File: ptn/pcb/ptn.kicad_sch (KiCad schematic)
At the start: 100 parts, among them IC1 ADP150AUJZ-3.3-R7, IC2 AZ1084CD-5.0TRG1, IC3 GRF5509, J1 TB002-500-04BE, J2 Conn_02x12_Counter_Clockwise, J3 NRF_CONN, J4 142-0701-801, J5 Conn_01x04, SW1 SW_Push, U1 NCP1117-3.3_SOT223, U2 ADF4351, U3 STM32F103C8T6, U4 MCP2551-I-SN, Y1 SIT5000AICGE-33E0-25.000000X, Y2 16MHz

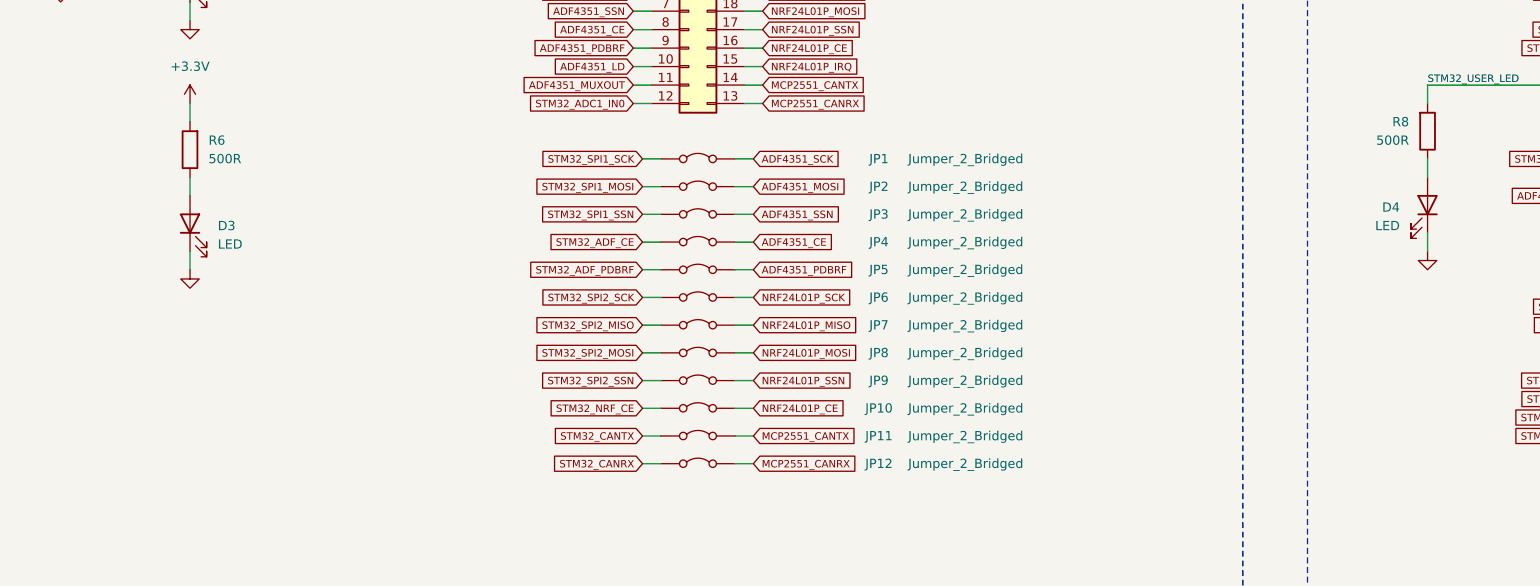
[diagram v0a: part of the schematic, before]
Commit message: Add correct LED resistances
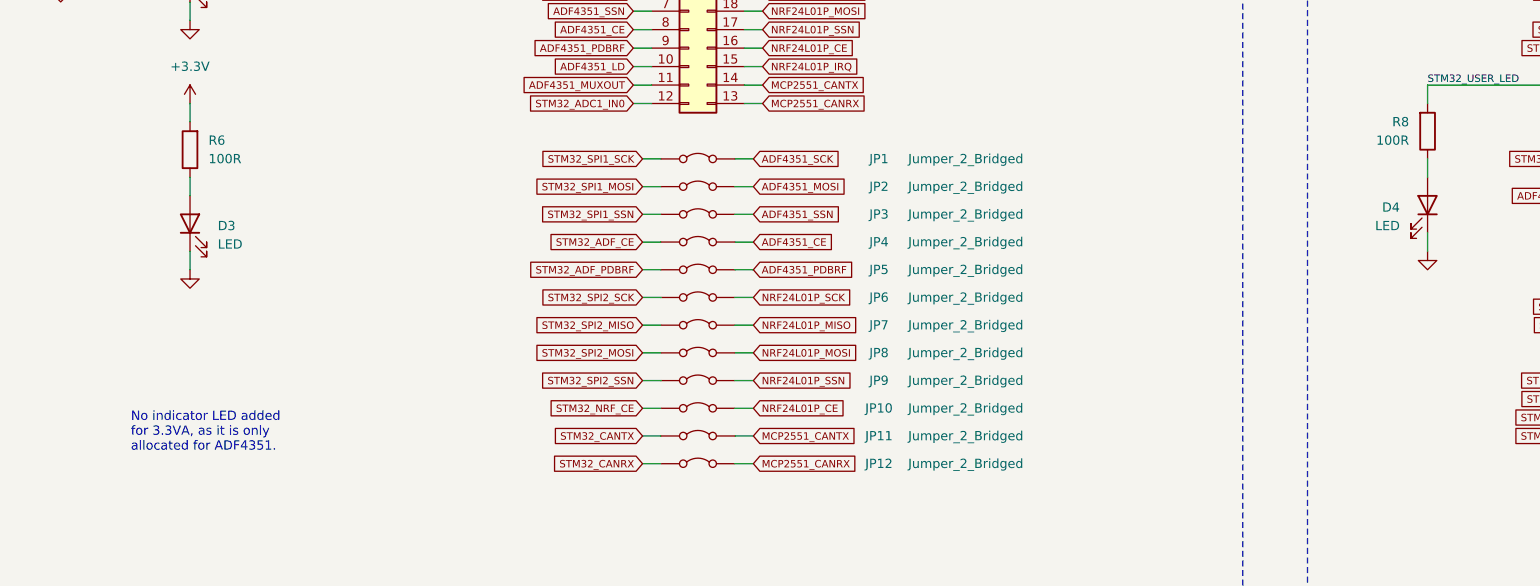
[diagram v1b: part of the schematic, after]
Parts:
- R6, R8: value 500R -> 100R
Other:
- note added: "No indicator LED added for 3.3VA, as it is only allocated for ADF4351."
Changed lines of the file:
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@@
 		)
 	)
+	(text "No indicator LED added\nfor 3.3VA, as it is only\nallocated for ADF4351."
+		(exclude_from_sim no)
+		(at 151.892 139.192 0)
+		(effects
+			(font
+				(size 1.27 1.27)
+			)
+			(justify left)
+		)
+	)
 	(text "Note: Check SW is needed or not."
 		(exclude_from_sim no)
@@
 			)
 		)
-		(property "Value" "500R"
+		(property "Value" "100R"
 			(at 327.66 99.0599 0)
 			(effects
@@
 			)
 		)
-		(property "Value" "500R"
+		(property "Value" "100R"
 			(at 162.56 101.5999 0)
 			(effects
@@
 			)
 		)
-		(property "Description" "Light emitting diode"
+		(property "Description" "Light emitting diode 150060VS55040"
 			(at 160.02 76.2 0)
 			(effects
@@
 			)
 		)
-		(property "Description" "Light emitting diode"
+		(property "Description" "Light emitting diode 150060VS55040"
 			(at 330.2 107.95 0)
 			(effects
@@
 			)
 		)
-		(property "Description" "Light emitting diode"
+		(property "Description" "Light emitting diode 150060VS55040"
 			(at 160.02 110.49 0)
 			(effects

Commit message: Footprint assignment
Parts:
- added C35, C36, C38, C42, C44, C46, C50, C51, C52: ~, symbol Device:C
- added C40: 0.1u, Capacitor_SMD:C_0402_1005Metric, symbol Device:C
- added R12: 0R, symbol Device:R
- C1, C5, C8: footprint (none) -> Capacitor_SMD:C_0805_2012Metric; Manufacturer_Name (none) -> Murata Electronics; Manufacturer_Part_Number (none) -> GRM21BR61E106KA73K; Mouser Part Number (none) -> 81-GRM21BR61E106KA3K
- C10: footprint (none) -> Capacitor_SMD:C_0805_2012Metric; Manufacturer_Name (none) -> Murata Electronics; Manufacturer_Part_Number (none) -> GRM21BR61E226ME44K; Mouser Part Number (none) -> 81-GRM21BR61E226ME4K
- C11, C12, C15, C17, C18, C19, C23, C24, C25, C31: footprint (none) -> Capacitor_SMD:C_0402_1005Metric; Manufacturer_Name (none) -> Murata Electronics; Manufacturer_Part_Number (none) -> GCM1555C1H100JA16J; Mouser Part Number (none) -> 81-GCM1555C1H100JA6J
- C13, C14, C16, C20, C21, C22, C26, C27, C28, C32: footprint (none) -> Capacitor_SMD:C_0402_1005Metric; Manufacturer_Name (none) -> Murata Electronics; Manufacturer_Part_Number (none) -> GRM155R71C104JA88J; Mouser Part Number (none) -> 81-GRM155R71C104JA8J
- C2, C9: footprint (none) -> Capacitor_SMD:C_0603_1608Metric; Manufacturer_Name (none) -> KEMET; Manufacturer_Part_Number (none) -> C0603C105K3PACTU; Mouser Part Number (none) -> 80-C0603C105K3P
- C29, C30: footprint (none) -> Capacitor_SMD:C_0603_1608Metric; Manufacturer_Name (none) -> KYOCERA AVX; Manufacturer_Part_Number (none) -> 06035A102JAT2A; Mouser Part Number (none) -> 581-06035A102J
- C3: footprint (none) -> Capacitor_SMD:C_0603_1608Metric; Manufacturer_Name (none) -> KYOCERA AVX; Manufacturer_Part_Number (none) -> 06031C272JAT2A; Mouser Part Number (none) -> 581-06031C272JAT2A
- C33: footprint (none) -> Capacitor_SMD:C_0402_1005Metric; Guerrilla ID (none) -> M4; Manufacturer_Name (none) -> Murata Electronics; Manufacturer_Part_Number (none) -> GJM1555C1H5R6WB01D; Mouser Part Number (none) -> 81-GJM1555C1H5R6WB1D
- C34: value 0.1u -> ~; Guerrilla ID (none) -> M5; now not fitted
- C37: renamed from C35; value 100n -> 0.1u; footprint (none) -> Capacitor_SMD:C_0402_1005Metric; Manufacturer_Name (none) -> Murata Electronics; Manufacturer_Part_Number (none) -> GRM155R71C104JA88J; Mouser Part Number (none) -> 81-GRM155R71C104JA8J
- C39: renamed from C37; footprint (none) -> Capacitor_SMD:C_0805_2012Metric; Manufacturer_Name (none) -> Murata Electronics; Manufacturer_Part_Number (none) -> GRM21BR61E106KA73K; Mouser Part Number (none) -> 81-GRM21BR61E106KA3K
- C4: footprint (none) -> Capacitor_SMD:C_0603_1608Metric; Manufacturer_Name (none) -> KEMET; Manufacturer_Part_Number (none) -> C0603C473J3RACTU; Mouser Part Number (none) -> 80-C0603C473J3R
- C41: renamed from C40; value 100n -> 0.1u; footprint (none) -> Capacitor_SMD:C_0402_1005Metric; Manufacturer_Name (none) -> Murata Electronics; Manufacturer_Part_Number (none) -> GRM155R71C104JA88J; Mouser Part Number (none) -> 81-GRM155R71C104JA8J
- C43: renamed from C42; value 100n -> 0.1u; footprint (none) -> Capacitor_SMD:C_0402_1005Metric; Manufacturer_Name (none) -> Murata Electronics; Manufacturer_Part_Number (none) -> GRM155R71C104JA88J; Mouser Part Number (none) -> 81-GRM155R71C104JA8J
- C45: renamed from C43; value 100n -> 0.1u; footprint (none) -> Capacitor_SMD:C_0402_1005Metric; Manufacturer_Name (none) -> Murata Electronics; Manufacturer_Part_Number (none) -> GRM155R71C104JA88J; Mouser Part Number (none) -> 81-GRM155R71C104JA8J
- C47: renamed from C38; footprint (none) -> Capacitor_SMD:C_0402_1005Metric; Guerrilla ID (none) -> M14; Manufacturer_Name (none) -> Murata Electronics; Manufacturer_Part_Number (none) -> GRM155R71C104JA88J; Mouser Part Number (none) -> 81-GRM155R71C104JA8J
- C48: renamed from C39; footprint (none) -> Capacitor_SMD:C_0402_1005Metric; Guerrilla ID (none) -> M15; Manufacturer_Name (none) -> Murata Electronics; Manufacturer_Part_Number (none) -> GRM1555C1H101FA01D; Mouser Part Number (none) -> 81-GRM1555C1H101FA1D
- C49: renamed from C44; value 100n -> 0.1u; footprint (none) -> Capacitor_SMD:C_0402_1005Metric; Manufacturer_Name (none) -> Murata Electronics; Manufacturer_Part_Number (none) -> GRM155R71C104JA88J; Mouser Part Number (none) -> 81-GRM155R71C104JA8J
- C53: renamed from C36; footprint (none) -> Capacitor_SMD:C_0402_1005Metric; Guerrilla ID (none) -> M22; Manufacturer_Name (none) -> Murata Electronics; Manufacturer_Part_Number (none) -> GJM1555C1H120FB01D; Mouser Part Number (none) -> 81-GJM1555C1H120FB1D
- C54: renamed from C41; footprint (none) -> Capacitor_SMD:C_0402_1005Metric; Guerrilla ID (none) -> M23; Manufacturer_Name (none) -> Murata Electronics; Manufacturer_Part_Number (none) -> GJM1555C1H200FB01D; Mouser Part Number (none) -> 81-GJM1555C1H200FB1D
- C55: renamed from C45; footprint (none) -> Capacitor_SMD:C_0603_1608Metric; Manufacturer_Name (none) -> KEMET; Manufacturer_Part_Number (none) -> C0603C103J5RAC7411; Mouser Part Number (none) -> 80-C0603C103J5R7411
- C56: renamed from C46; footprint (none) -> Capacitor_SMD:C_0603_1608Metric; Manufacturer_Name (none) -> KEMET; Manufacturer_Part_Number (none) -> C0603C105K3PACTU; Mouser Part Number (none) -> 80-C0603C105K3P
- C57: renamed from C47; footprint (none) -> Capacitor_SMD:C_0402_1005Metric; Manufacturer_Name (none) -> Murata Electronics; Manufacturer_Part_Number (none) -> GCM1555C1H100JA16J; Mouser Part Number (none) -> 81-GCM1555C1H100JA6J
- C58: renamed from C48; footprint (none) -> Capacitor_SMD:C_0603_1608Metric; Manufacturer_Name (none) -> KEMET; Manufacturer_Part_Number (none) -> C0603C105K3PACTU; Mouser Part Number (none) -> 80-C0603C105K3P
- C59: renamed from C49; footprint (none) -> Capacitor_SMD:C_0402_1005Metric; Manufacturer_Name (none) -> Murata Electronics; Manufacturer_Part_Number (none) -> GCM1555C1H100JA16J; Mouser Part Number (none) -> 81-GCM1555C1H100JA6J
- C6: footprint (none) -> Capacitor_SMD:C_0402_1005Metric; Manufacturer_Name (none) -> Murata Electronics; Manufacturer_Part_Number (none) -> GRM1555C1H101FA01D; Mouser Part Number (none) -> 81-GRM1555C1H101FA1D
- C7: footprint (none) -> Capacitor_SMD:C_0603_1608Metric; Manufacturer_Name (none) -> KEMET; Manufacturer_Part_Number (none) -> C0603C122J5RACTU; Mouser Part Number (none) -> 80-C0603C122J5R
- D1: Manufacturer_Name (none) -> ROHM Semiconductor; Manufacturer_Part_Number (none) -> RF302LAM2STR; Mouser Part Number (none) -> 755-RF302LAM2STR
- D2, D3, D4: footprint (none) -> LED_SMD:LED_0603_1608Metric; Manufacturer_Name (none) -> Wurth Elektronik; Manufacturer_Part_Number (none) -> 150060VS55040; Mouser Part Number (none) -> 710-150060VS55040
- FB1: footprint (none) -> Inductor_SMD:L_0603_1608Metric; Manufacturer_Name (none) -> Bussmann / Eaton; Manufacturer_Part_Number (none) -> MFBM1V1608-121-R; Mouser Part Number (none) -> 704-MFBM1V1608-121-R
- J2: footprint (none) -> Connector_PinHeader_2.54mm:PinHeader_2x12_P2.54mm_Vertical
- J3: footprint (none) -> Connector_PinSocket_2.54mm:PinSocket_2x04_P2.54mm_Vertical
- J4: renamed from J5; footprint (none) -> Connector_PinHeader_2.54mm:PinHeader_1x04_P2.54mm_Vertical
- J5: renamed from J4; footprint 142-0701-851 -> project_footprint_library:142-0701-851
- JP1, JP10, JP11, JP12, JP2, JP3, JP4, JP5, JP6, JP7, JP8, JP9: footprint (none) -> Connector_PinHeader_2.54mm:PinHeader_1x02_P2.54mm_Vertical
- JP13: footprint (none) -> Connector_PinHeader_2.54mm:PinHeader_1x03_P2.54mm_Vertical
- L1: Guerrilla ID (none) -> L1
- L2: Guerrilla ID (none) -> M2
- L3: Guerrilla ID (none) -> M18
- R10: Guerrilla ID (none) -> M1
- R11: Guerrilla ID (none) -> M3
- R13: renamed from R12; Guerrilla ID (none) -> M9
- R14: renamed from R13; Guerrilla ID (none) -> M11
- R15: renamed from R14; Guerrilla ID (none) -> M12
- SW1: footprint (none) -> Button_Switch_SMD:SW_SPST_Omron_B3FS-100xP; Manufacturer_Name (none) -> Omron Electronics; Manufacturer_Part_Number (none) -> B3FS-1002P; Mouser Part Number (none) -> 653-B3FS-1002P
- U1: Manufacturer_Name (none) -> onsemi; Manufacturer_Part_Number (none) -> NCP1117ST33T3G; Mouser Part Number (none) -> 863-NCP1117ST33T3G
- U2: Manufacturer_Name (none) -> Analog Devices; Manufacturer_Part_Number (none) -> ADF4351BCPZ-RL7; Mouser Part Number (none) -> 584-ADF4351BCPZ-R7
- U3: renamed from U4; Manufacturer_Name (none) -> Microchip Technology; Manufacturer_Part_Number (none) -> MCP2551-I/SN; Mouser Part Number (none) -> 579-MCP2551-I/SN
- U4: renamed from U3; Manufacturer_Name (none) -> STMicroelectronics; Manufacturer_Part_Number (none) -> STM32F103C8T6; Mouser Part Number (none) -> 511-STM32F103C8T6
- Y1: Manufacturer_Part_Number SIT5000AICGE-33N0-25.000000X -> SIT5000AICGE-33E0-25.000000X; Mouser Part Number 788-5000AICGE3N0-25X -> 788-5000AICGE3E0-25X
- Y2: Manufacturer_Name (none) -> Wurth Elektronik; Manufacturer_Part_Number (none) -> 830108288709; Mouser Part Number (none) -> 710-830108288709
- renumbered R15 to R16, R9 to R7, R7 to R8, R8 to R9
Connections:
- net +5V: now also R10.2, R15.1, C40.2, C46.1; no longer C34.2, R10.1, R15.2
- net GND: now also C34.2, C35.2, C36.2, C38.2, C40.1, C42.1, C44.1, C46.2, C50.1, C51.1, C52.1, R12.1; no longer C34.1, IC3.15 (GND/NC_8)
- net GRF5509_VEN1: now also C34.1, R10.1; no longer R10.2
- net GRF5509_VEN2: now also C36.1
- net at C53.2, C54.1, IC3.10 (RF_OUT/VCC2_2)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: now also C42.2, C44.2, C50.2, C51.2, C52.2
- net at IC3.12 (BIAS): now also R15.2; no longer R15.1
- net at C33.2, IC3.3 (RF_IN_1), IC3.4 (RF_IN_2): now also C35.1
- new net: C38.1, IC3.15 (GND/NC_8), R12.2
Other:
- note added: "CL = 2*(CL0-Cs)=2*(10-5)pF=10pF"
- note added: "PDET pin should be connected to GND or N/C"
- note added: "Use 1nF if also using inductor"
- moved on the sheet: C33, C47, C48, C53, C54, IC3, J3, J5, L1, L2, L3, R11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

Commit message: Complete footprint assignment
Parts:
- added L4: 7.5n, Inductor_SMD:L_0402_1005Metric, symbol Device:L
- C34, C35, C36, C38, C42, C44, C46, C50, C51, C52: footprint (none) -> Capacitor_SMD:C_0402_1005Metric
- L1, L2: footprint (none) -> Inductor_SMD:L_0402_1005Metric; Manufacturer_Name (none) -> Murata Electronics; Manufacturer_Part_Number (none) -> LQG15WH6N8G02D; Mouser Part Number (none) -> 81-LQG15WH6N8G02D
- L3: footprint (none) -> Inductor_SMD:L_0603_1608Metric; Manufacturer_Name (none) -> Murata Electronics; Manufacturer_Part_Number (none) -> LQW18AN24NG80D; Mouser Part Number (none) -> 81-LQW18AN24NG80D
- R1: footprint (none) -> Resistor_SMD:R_0603_1608Metric; Manufacturer_Name (none) -> Vishay / Dale; Manufacturer_Part_Number (none) -> CRCW06035K10FKEC; Mouser Part Number (none) -> 71-CRCW06035K10FKEC
- R10: footprint (none) -> Resistor_SMD:R_0402_1005Metric; Manufacturer_Name (none) -> Panasonic; Manufacturer_Part_Number (none) -> ERJ-2GEJ332X; Mouser Part Number (none) -> 667-ERJ-2GEJ332X
- R11: footprint (none) -> Resistor_SMD:R_0402_1005Metric; Manufacturer_Name (none) -> Panasonic; Manufacturer_Part_Number (none) -> ERJ-2GEJ682X; Mouser Part Number (none) -> 667-ERJ-2GEJ682X
- R12, R13, R14, R15: footprint (none) -> Resistor_SMD:R_0402_1005Metric; Manufacturer_Name (none) -> Vishay / Dale; Manufacturer_Part_Number (none) -> RCS04020000Z0ED; Mouser Part Number (none) -> 71-RCS04020000Z0ED
- R16: footprint (none) -> Resistor_SMD:R_0603_1608Metric; Manufacturer_Name (none) -> YAGEO; Manufacturer_Part_Number (none) -> RT0603FRE1310KL; Mouser Part Number (none) -> 603-RT0603FRE1310KL
- R2: footprint (none) -> Resistor_SMD:R_0603_1608Metric; Manufacturer_Name (none) -> YAGEO; Manufacturer_Part_Number (none) -> RT0603BRE0750RL; Mouser Part Number (none) -> 603-RT0603BRE0750RL
- R3: footprint (none) -> Resistor_SMD:R_0603_1608Metric; Manufacturer_Name (none) -> YAGEO; Manufacturer_Part_Number (none) -> RT0603DRE07360RL; Mouser Part Number (none) -> 603-RT0603DRE07360RL
- R4, R7: footprint (none) -> Resistor_SMD:R_0603_1608Metric; Manufacturer_Name (none) -> YAGEO; Manufacturer_Part_Number (none) -> RC0603FR-101KL; Mouser Part Number (none) -> 603-RC0603FR-101KL
- R5: value 500R -> 250R; footprint (none) -> Resistor_SMD:R_0603_1608Metric; Manufacturer_Name (none) -> YAGEO; Manufacturer_Part_Number (none) -> RT0603BRE07250RL; Mouser Part Number (none) -> 603-RT0603BRE07250RL
- R6, R9: footprint (none) -> Resistor_SMD:R_0603_1608Metric; Manufacturer_Name (none) -> YAGEO; Manufacturer_Part_Number (none) -> RT0603DRE07100RL; Mouser Part Number (none) -> 603-RT0603DRE07100RL
- R8: footprint (none) -> Resistor_SMD:R_0603_1608Metric; Manufacturer_Name (none) -> YAGEO; Manufacturer_Part_Number (none) -> RT0603FRE102KL; Mouser Part Number (none) -> 603-RT0603FRE102KL
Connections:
- net +3.3VA: now also L4.1
- net ADF4351_RFOUTA+: now also L4.2

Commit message: Start PCB layout
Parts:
- removed JP1, JP10, JP11, JP12, JP2, JP3, JP4, JP5, JP6, JP7, JP8, JP9: Jumper_2_Bridged, Connector_PinHeader_2.54mm:PinHeader_1x02_P2.54mm_Vertical, symbol Jumper:Jumper_2_Bridged
- added J6: IO_CTRL_JP_BANK, Connector_PinHeader_2.54mm:PinHeader_2x12_P2.54mm_Vertical, symbol Connector_Generic:Conn_02x12_Counter_Clockwise
- added R17: 120R, Resistor_SMD:R_0603_1608Metric, symbol Device:R
- J2: value Conn_02x12_Counter_Clockwise -> IO_BREAKOUT_CONN
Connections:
- net ADF4351_CE: now also J2.17 (Pin_17), J6.21 (Pin_21); no longer J2.8 (Pin_8)
- net ADF4351_LD: now also J2.15 (Pin_15); no longer J2.10 (Pin_10)
- net ADF4351_MOSI: now also J2.19 (Pin_19), J6.23 (Pin_23); no longer J2.6 (Pin_6)
- net ADF4351_MUXOUT: now also J2.14 (Pin_14); no longer J2.11 (Pin_11)
- net ADF4351_PDBRF: now also J2.16 (Pin_16), J6.20 (Pin_20); no longer J2.9 (Pin_9)
- net ADF4351_SCK: now also J2.20 (Pin_20), J6.24 (Pin_24); no longer J2.5 (Pin_5)
- net ADF4351_SSN: now also J2.18 (Pin_18), J6.22 (Pin_22); no longer J2.7 (Pin_7)
- net CANH: now also J1.4, R17.1; no longer J1.3
- net CANL: now also J1.3, R17.2; no longer J1.4
- net MCP2551_CANRX: now also J2.12 (Pin_12), J6.13 (Pin_13); no longer J2.13 (Pin_13)
- net MCP2551_CANTX: now also J2.11 (Pin_11), J6.14 (Pin_14); no longer J2.14 (Pin_14)
- net NRF24L01P_CE: now also J2.9 (Pin_9), J6.15 (Pin_15); no longer J2.16 (Pin_16)
- net NRF24L01P_IRQ: now also J2.10 (Pin_10); no longer J2.15 (Pin_15)
- net NRF24L01P_MISO: now also J2.6 (Pin_6), J6.18 (Pin_18); no longer J2.19 (Pin_19)
- net NRF24L01P_MOSI: now also J2.7 (Pin_7), J6.17 (Pin_17); no longer J2.18 (Pin_18)
- net NRF24L01P_SCK: now also J2.5 (Pin_5), J6.19 (Pin_19); no longer J2.20 (Pin_20)
- net NRF24L01P_SSN: now also J2.8 (Pin_8), J6.16 (Pin_16); no longer J2.17 (Pin_17)
- net STM32_ADC1_IN0: now also J2.13 (Pin_13); no longer J2.12 (Pin_12)
- net STM32_ADF_CE: now also J6.4 (Pin_4)
- net STM32_ADF_PDBRF: now also J6.5 (Pin_5)
- net STM32_CANRX: now also J6.12 (Pin_12)
- net STM32_CANTX: now also J6.11 (Pin_11)
- net STM32_NRF_CE: now also J6.10 (Pin_10)
- net STM32_SPI1_MOSI: now also J6.2 (Pin_2)
- net STM32_SPI1_SCK: now also J6.1 (Pin_1)
- net STM32_SPI1_SSN: now also J6.3 (Pin_3)
- net STM32_SPI2_MISO: now also J6.7 (Pin_7)
- net STM32_SPI2_MOSI: now also J6.8 (Pin_8)
- net STM32_SPI2_SCK: now also J6.6 (Pin_6)
- net STM32_SPI2_SSN: now also J6.9 (Pin_9)

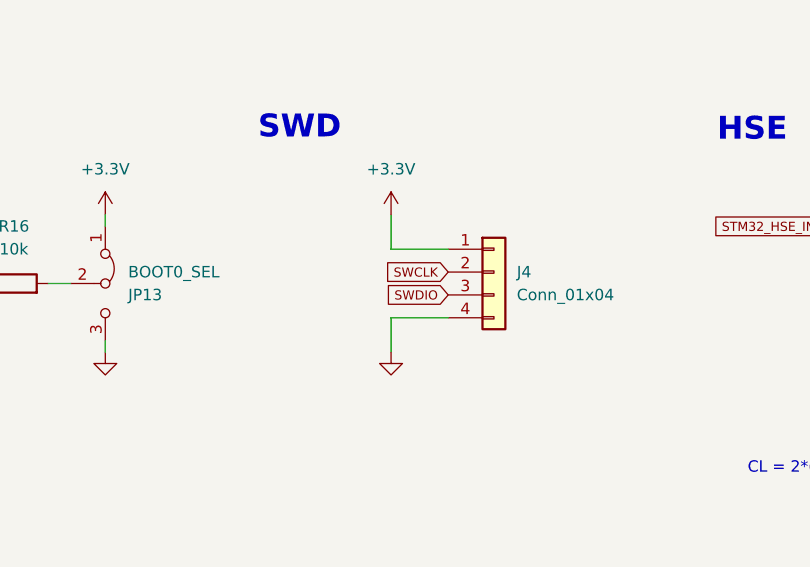
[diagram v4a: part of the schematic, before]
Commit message: Organize subsystem layouts
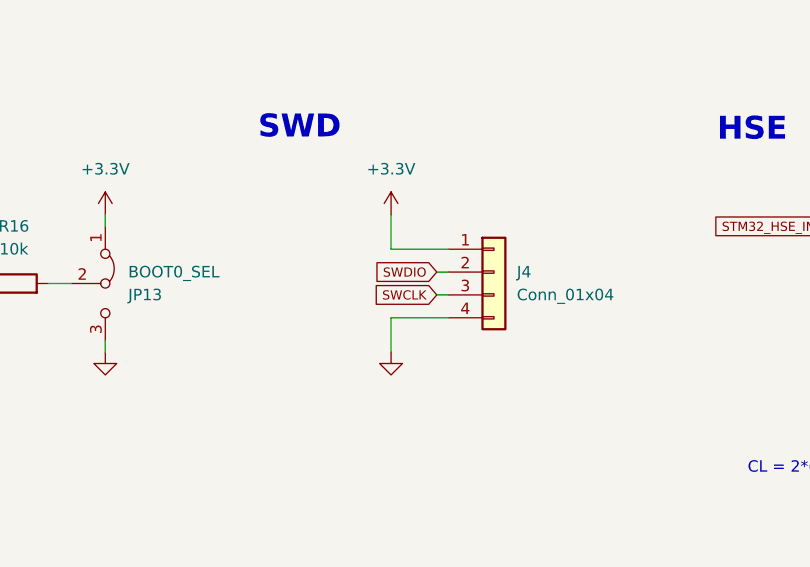
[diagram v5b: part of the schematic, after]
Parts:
- C55: footprint Capacitor_SMD:C_0603_1608Metric -> Capacitor_SMD:C_0402_1005Metric; Manufacturer_Part_Number C0603C103J5RAC7411 -> C0402C103J8RACTU; Mouser Part Number 80-C0603C103J5R7411 -> 80-C0402C103J8RACTU
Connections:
- net SWCLK: now also J4.3 (Pin_3); no longer J4.2 (Pin_2)
- net SWDIO: now also J4.2 (Pin_2); no longer J4.3 (Pin_3)
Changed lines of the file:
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@@
 	(wire
 		(pts
+			(xy 560.07 124.46) (xy 561.34 124.46)
+		)
+		(stroke
+			(width 0)
+			(type default)
+		)
+	)
+	(wire
+		(pts
 			(xy 220.98 86.36) (xy 223.52 86.36)
 		)
@@
 	(wire
 		(pts
+			(xy 560.07 121.92) (xy 561.34 121.92)
+		)
+		(stroke
+			(width 0)
+			(type default)
+		)
+	)
+	(wire
+		(pts
 			(xy 392.43 86.36) (xy 394.97 86.36)
 		)
@@
 		)
 	)
-	(global_label "SWDIO"
-		(shape input)
-		(at 561.34 124.46 180)
-		(fields_autoplaced yes)
-		(effects
-			(font
-				(size 1.016 1.016)
-			)
-			(justify right)
-		)
-		(property "Intersheetrefs" "${INTERSHEET_REFS}"
-			(at 554.2592 124.46 0)
-			(effects
-				(font
-					(size 1.27 1.27)
-				)
-				(justify right)
-				(hide yes)
-			)
-		)
-	)
 	(global_label "STM32_ADF_PDBRF"
 		(shape input)
@@
 		)
 	)
-	(global_label "SWCLK"
-		(shape input)
-		(at 561.34 121.92 180)
-		(fields_autoplaced yes)
-		(effects
-			(font
-				(size 1.016 1.016)
-			)
-			(justify right)
-		)
-		(property "Intersheetrefs" "${INTERSHEET_REFS}"
-			(at 552.1258 121.92 0)
-			(effects
-				(font
-					(size 1.27 1.27)
-				)
-				(justify right)
-				(hide yes)
-			)
-		)
-	)
 	(global_label "NRF24L01P_MISO"
 		(shape input)
@@
 		)
 	)
+	(global_label "SWCLK"
+		(shape input)
+		(at 560.07 124.46 180)
+		(fields_autoplaced yes)
+		(effects
+			(font
+				(size 1.016 1.016)
+			)
+			(justify right)
+		)
+		(property "Intersheetrefs" "${INTERSHEET_REFS}"
+			(at 550.8558 124.46 0)
+			(effects
+				(font
+					(size 1.27 1.27)
+				)
+				(justify right)
+				(hide yes)
+			)
+		)
+	)
 	(global_label "STM32_NRF_CE"
 		(shape input)
@@
 		)
 	)
+	(global_label "SWDIO"
+		(shape input)
+		(at 560.07 121.92 180)
+		(fields_autoplaced yes)
+		(effects
+			(font
+				(size 1.016 1.016)
+			)
+			(justify right)
+		)
+		(property "Intersheetrefs" "${INTERSHEET_REFS}"
+			(at 552.9892 121.92 0)
+			(effects
+				(font
+					(size 1.27 1.27)
+				)
+				(justify right)
+				(hide yes)
+			)
+		)
+	)
 	(global_label "STM32_SPI1_MOSI"
 		(shape input)
@@
 			)
 		)
-		(property "Footprint" "Capacitor_SMD:C_0603_1608Metric"
+		(property "Footprint" "Capacitor_SMD:C_0402_1005Metric"
 			(at 585.7748 73.66 0)
 			(effects
@@
 			)
 		)
-		(property "Manufacturer_Part_Number" "C0603C103J5RAC7411"
+		(property "Manufacturer_Part_Number" "C0402C103J8RACTU"
 			(at 586.74 77.47 0)
 			(effects
@@
 			)
 		)
-		(property "Mouser Part Number" "80-C0603C103J5R7411"
+		(property "Mouser Part Number" "80-C0402C103J8RACTU"
 			(at 586.74 77.47 0)
 			(effects
